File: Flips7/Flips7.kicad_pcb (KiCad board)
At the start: 2 copper layers, 100 x 100 mm, 20 parts, among them CN1 Conn_02x17_Odd_Even, CN2 Conn_02x17_Odd_Even, U1 FP2800A, U2 FP2800A, U3 FP2800A

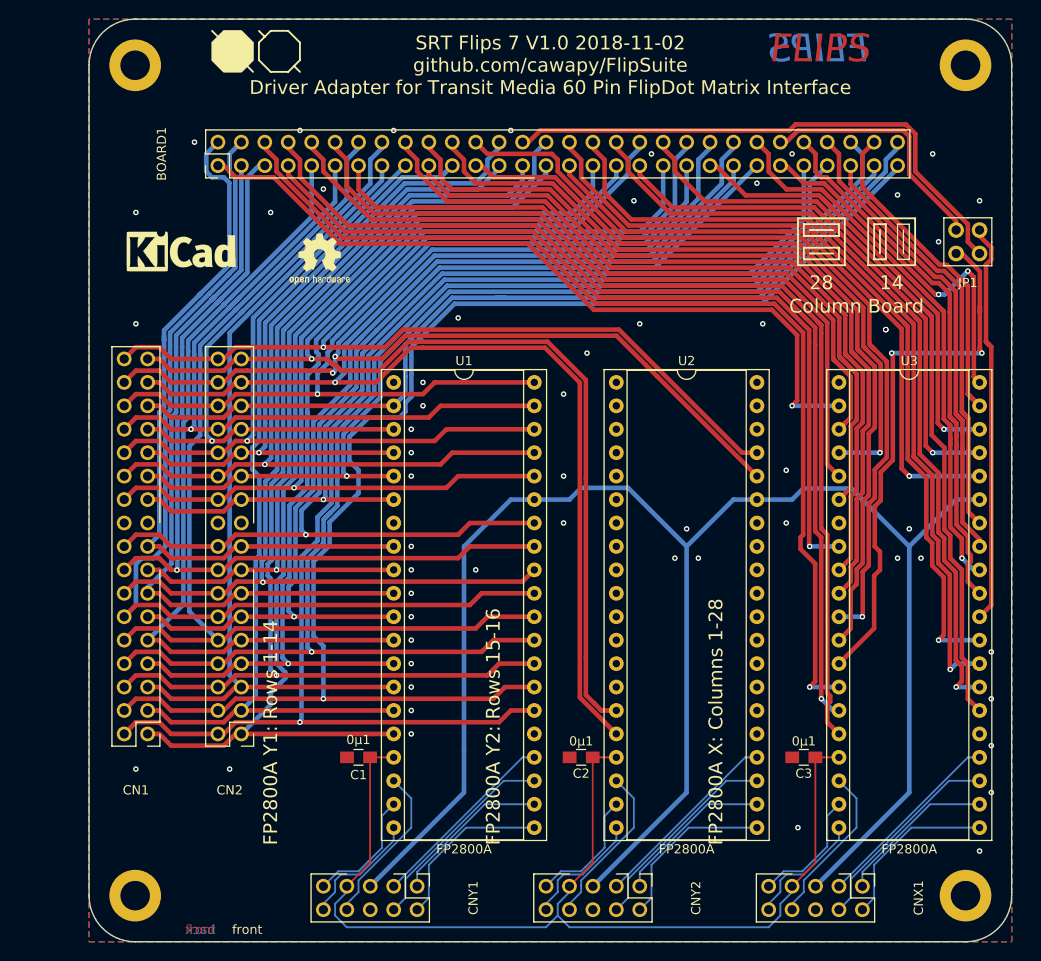
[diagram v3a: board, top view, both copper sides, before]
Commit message: moving text, adding lines to visually group driver ics and corresponding connectors
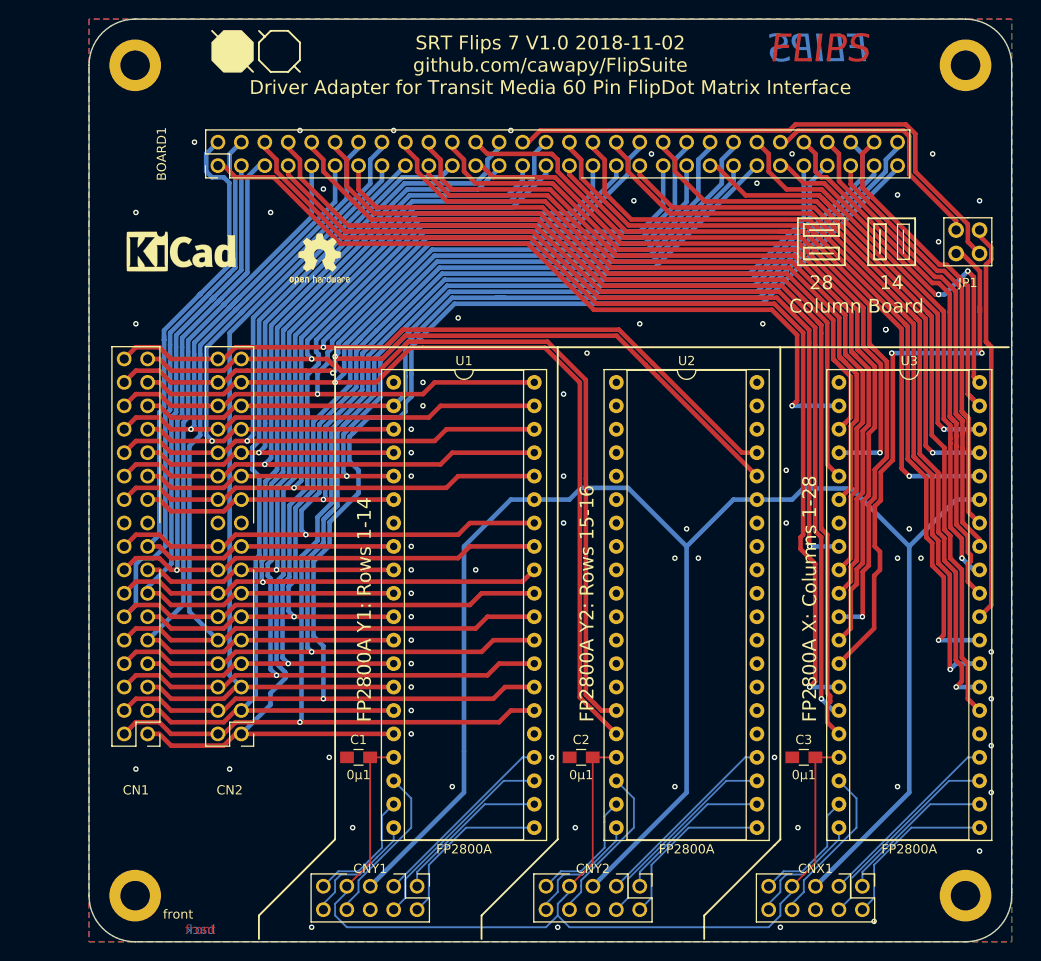
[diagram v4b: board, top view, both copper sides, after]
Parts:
- moved REF*** 48.3 mm to (30.5, 110.5)
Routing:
- net /GND: vias 56 -> 68
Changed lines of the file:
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@@
   (general
     (thickness 1.6)
-    (drawings 64)
-    (tracks 1399)
+    (drawings 76)
+    (tracks 1411)
     (zones 0)
     (modules 20)
@@
   )
   (layers
-    (0 F.Cu signal hide)
+    (0 F.Cu signal)
     (31 B.Cu signal)
     (32 B.Adhes user)
@@
     (34 B.Paste user)
     (35 F.Paste user)
-    (36 B.SilkS user hide)
-    (37 F.SilkS user hide)
+    (36 B.SilkS user)
+    (37 F.SilkS user)
     (38 B.Mask user)
     (39 F.Mask user)
@@
     (46 B.CrtYd user)
     (47 F.CrtYd user)
-    (48 B.Fab user hide)
-    (49 F.Fab user hide)
+    (48 B.Fab user)
+    (49 F.Fab user)
   )
   (setup
@@
     (tags "capacitor 0805")
     (attr smd)
-    (fp_text reference C2 (at 0 -1.75 180) (layer F.SilkS)
+    (fp_text reference C2 (at 0 1.905 180) (layer F.SilkS)
       (effects (font (size 1 1) (thickness 0.15)))
     )
-    (fp_text value 0µ1 (at 0 1.75 180) (layer F.SilkS)
+    (fp_text value 0µ1 (at 0 -1.905 180) (layer F.SilkS)
       (effects (font (size 1 1) (thickness 0.15)))
     )
@@
     (fp_line (start 1 0.62) (end -1 0.62) (layer F.Fab) (width 0.1))
     (fp_line (start -1 0.62) (end -1 -0.62) (layer F.Fab) (width 0.1))
-    (fp_text user %R (at 0 -1.75 180) (layer F.Fab)
+    (fp_text user %R (at 0 1.905 180) (layer F.Fab)
       (effects (font (size 1 1) (thickness 0.15)))
     )
@@
     (tags "capacitor 0805")
     (attr smd)
-    (fp_text reference C3 (at 0 -1.75 180) (layer F.SilkS)
+    (fp_text reference C3 (at 0 1.905 180) (layer F.SilkS)
       (effects (font (size 1 1) (thickness 0.15)))
     )
-    (fp_text value 0µ1 (at 0 1.75 180) (layer F.SilkS)
+    (fp_text value 0µ1 (at 0 -1.905 180) (layer F.SilkS)
       (effects (font (size 1 1) (thickness 0.15)))
     )
@@
     (fp_line (start 1 0.62) (end -1 0.62) (layer F.Fab) (width 0.1))
     (fp_line (start -1 0.62) (end -1 -0.62) (layer F.Fab) (width 0.1))
-    (fp_text user %R (at 0 -1.75 180) (layer F.Fab)
+    (fp_text user %R (at 0 1.905 180) (layer F.Fab)
       (effects (font (size 1 1) (thickness 0.15)))
     )
@@
   )
   (module Symbols:WEEE-Logo_4.2x6mm_SilkScreen (layer B.Cu)
-    (at 78.105 118.745 180)
+    (at 30.48 110.49 180)
     (descr "Waste Electrical and Electronic Equipment Directive")
     (tags "Logo WEEE")
@@
     (tags "capacitor 0805")
     (attr smd)
-    (fp_text reference C1 (at 0 1.905) (layer F.SilkS)
+    (fp_text reference C1 (at 0 -1.905) (layer F.SilkS)
       (effects (font (size 1 1) (thickness 0.15)))
     )
-    (fp_text value 0µ1 (at -0.02 -1.905) (layer F.SilkS)
+    (fp_text value 0µ1 (at 0 1.905) (layer F.SilkS)
       (effects (font (size 1 1) (thickness 0.15)))
     )
@@
     (fp_line (start 1 0.62) (end -1 0.62) (layer F.Fab) (width 0.1))
     (fp_line (start -1 0.62) (end -1 -0.62) (layer F.Fab) (width 0.1))
-    (fp_text user %R (at 0 -1.75) (layer F.Fab)
+    (fp_text user %R (at 0 -1.905) (layer F.Fab)
       (effects (font (size 1 1) (thickness 0.15)))
     )
@@
     (descr "Through hole shrouded angle pin header, 2x05, 2.54mm pitch, double rows, conventional numbering")
     (tags "Through hole shrouded angle pin header THT 2x05 2.54mm double row, conventional numbering")
-    (fp_text reference CNX1 (at 1.27 -6.096 270) (layer F.SilkS)
+    (fp_text reference CNX1 (at -1.905 5.08) (layer F.SilkS)
       (effects (font (size 1 1) (thickness 0.15)))
     )
@@
     (descr "Through hole shrouded angle pin header, 2x05, 2.54mm pitch, double rows, conventional numbering")
     (tags "Through hole shrouded angle pin header THT 2x05 2.54mm double row, conventional numbering")
-    (fp_text reference CNY1 (at 1.27 -6.096 270) (layer F.SilkS)
+    (fp_text reference CNY1 (at -1.905 5.08) (layer F.SilkS)
       (effects (font (size 1 1) (thickness 0.15)))
     )
@@
     (descr "Through hole shrouded angle pin header, 2x05, 2.54mm pitch, double rows, conventional numbering")
     (tags "Through hole shrouded angle pin header THT 2x05 2.54mm double row, conventional numbering")
-    (fp_text reference CNY2 (at 1.27 -6.096 270) (layer F.SilkS)
+    (fp_text reference CNY2 (at -1.905 5.08) (layer F.SilkS)
       (effects (font (size 1 1) (thickness 0.15)))
     )
@@
     (pad 1 thru_hole circle (at 0 0) (size 5.6 5.6) (drill 3.2) (layers *.Cu *.Mask))
   )
+  (gr_line (start 52.07 60.96) (end 125.095 60.96) (angle 90) (layer F.SilkS) (width 0.2))
+  (gr_line (start 52.07 114.3) (end 52.07 60.96) (angle 90) (layer F.SilkS) (width 0.2))
+  (gr_line (start 43.815 122.555) (end 52.07 114.3) (angle 90) (layer F.SilkS) (width 0.2))
+  (gr_line (start 43.815 125.095) (end 43.815 122.555) (angle 90) (layer F.SilkS) (width 0.2))
+  (gr_line (start 76.2 114.3) (end 76.2 60.96) (angle 90) (layer F.SilkS) (width 0.2))
+  (gr_line (start 67.945 122.555) (end 76.2 114.3) (angle 90) (layer F.SilkS) (width 0.2))
+  (gr_line (start 67.945 125.095) (end 67.945 122.555) (angle 90) (layer F.SilkS) (width 0.2))
+  (gr_line (start 100.33 114.3) (end 100.33 60.96) (angle 90) (layer F.SilkS) (width 0.2))
+  (gr_line (start 99.695 114.935) (end 100.33 114.3) (angle 90) (layer F.SilkS) (width 0.2))
+  (gr_line (start 92.075 123.825) (end 92.075 125.095) (angle 90) (layer F.SilkS) (width 0.2))
+  (gr_line (start 92.075 122.555) (end 92.075 123.825) (angle 90) (layer F.SilkS) (width 0.2))
+  (gr_line (start 99.695 114.935) (end 92.075 122.555) (angle 90) (layer F.SilkS) (width 0.2))
   (gr_text "Column Board" (at 108.585 56.515) (layer F.SilkS)
     (effects (font (size 1.5 1.5) (thickness 0.3)))
   )
-  (gr_text "FP2800A X: Columns 1-28" (at 93.345 114.935 90) (layer F.SilkS)
+  (gr_text "FP2800A X: Columns 1-28" (at 103.505 101.6 90) (layer F.SilkS)
     (effects (font (size 1.5 1.5) (thickness 0.3)) (justify left))
   )
@@
   (gr_arc (start 120.4 30.4) (end 125.4 30.4) (angle -90) (layer Edge.Cuts) (width 0.15))
   (gr_arc (start 30.4 30.4) (end 30.4 25.4) (angle -90) (layer Edge.Cuts) (width 0.15))
-  (gr_text back (at 42.545 124.079) (layer B.SilkS)
+  (gr_text back (at 35.052 122.428) (layer B.SilkS)
     (effects (font (size 1 1) (thickness 0.25)) (justify mirror))
   )
@@
     (effects (font (size 1 1) (thickness 0.25)) (justify mirror))
   )
-  (gr_text front (at 42.545 124.079) (layer F.SilkS)
+  (gr_text front (at 35.052 122.428) (layer F.SilkS)
     (effects (font (size 1 1) (thickness 0.25)))
   )
@@
     (effects (font (size 1.5 1.5) (thickness 0.3)))
   )
-  (gr_text "FP2800A Y1: Rows 1-14" (at 45.085 114.935 90) (layer F.SilkS)
+  (gr_text "FP2800A Y1: Rows 1-14" (at 55.245 101.6 90) (layer F.SilkS)
     (effects (font (size 1.5 1.5) (thickness 0.3)) (justify left))
   )
-  (gr_text "FP2800A Y2: Rows 15-16" (at 69.215 114.935 90) (layer F.SilkS)
+  (gr_text "FP2800A Y2: Rows 15-16" (at 79.375 101.6 90) (layer F.SilkS)
     (effects (font (size 1.5 1.5) (thickness 0.3)) (justify left))
   )
@@
   (via (at 76.835 74.93) (size 0.6) (drill 0.3) (layers F.Cu B.Cu) (net 112))
   (via (at 100.965 80.01) (size 0.6) (drill 0.3) (layers F.Cu B.Cu) (net 112))
+  (via (at 51.435 105.41) (size 0.6) (drill 0.3) (layers F.Cu B.Cu) (net 112))
+  (via (at 75.565 105.41) (size 0.6) (drill 0.3) (layers F.Cu B.Cu) (net 112))
+  (via (at 99.695 105.41) (size 0.6) (drill 0.3) (layers F.Cu B.Cu) (net 112))
+  (via (at 78.105 113.03) (size 0.6) (drill 0.3) (layers F.Cu B.Cu) (net 112))
+  (via (at 53.975 113.03) (size 0.6) (drill 0.3) (layers F.Cu B.Cu) (net 112))
+  (via (at 64.77 108.585) (size 0.6) (drill 0.3) (layers F.Cu B.Cu) (net 112))
+  (via (at 88.9 108.585) (size 0.6) (drill 0.3) (layers F.Cu B.Cu) (net 112))
+  (via (at 113.03 108.585) (size 0.6) (drill 0.3) (layers F.Cu B.Cu) (net 112))
+  (via (at 110.49 123.19) (size 0.6) (drill 0.3) (layers F.Cu B.Cu) (net 112))
+  (via (at 100.33 123.825) (size 0.6) (drill 0.3) (layers F.Cu B.Cu) (net 112))
+  (via (at 76.2 123.825) (size 0.6) (drill 0.3) (layers F.Cu B.Cu) (net 112))
+  (via (at 49.53 123.825) (size 0.6) (drill 0.3) (layers F.Cu B.Cu) (net 112))
   (segment (start 66.04 104.775) (end 66.04 82.55) (width 0.5) (layer B.Cu) (net 113) (status 10))
   (segment (start 71.12 77.47) (end 73.66 77.47) (width 0.5) (layer B.Cu) (net 113) (status 20))

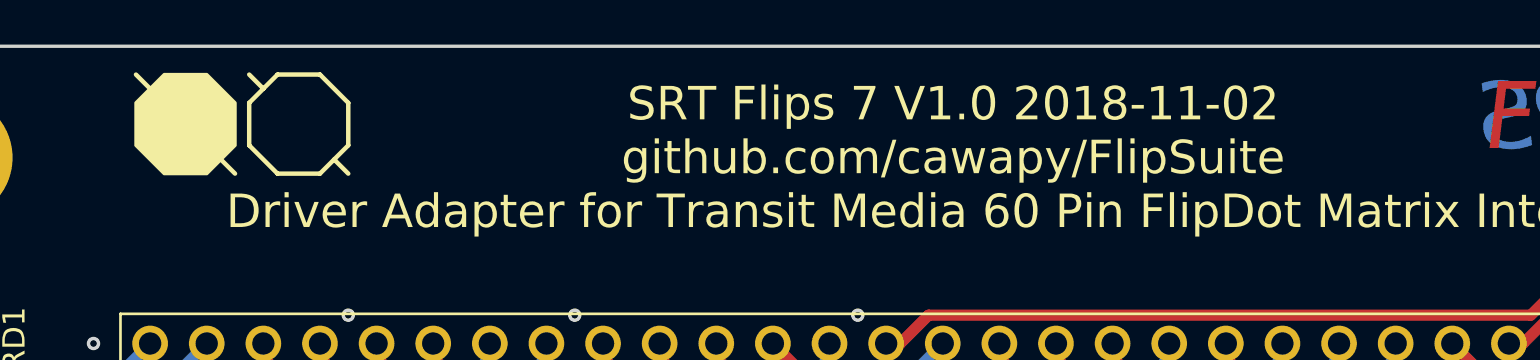
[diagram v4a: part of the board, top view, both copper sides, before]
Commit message: Adding Flips Logo
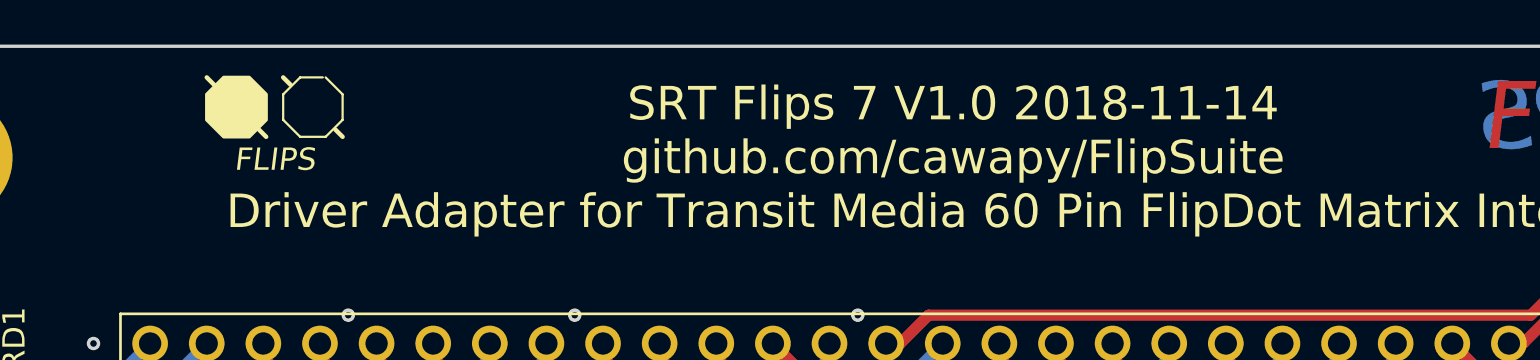
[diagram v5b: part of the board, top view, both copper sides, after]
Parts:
- added REF**: FlipsLogo-Mittel, Own:FlipsLogo-Mittel, F.Cu at (45.0, 29.5)
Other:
- board text added: "SRT Flips 7 V1.0 2018-11-14 github.com/cawapy/FlipSuite Driver Adapter for Transit Media 60 Pin FlipDot Matrix Interface"
- board text removed: "SRT Flips 7 V1.0 2018-11-02 github.com/cawapy/FlipSuite Driver Adapter for Transit Media 60 Pin FlipDot Matrix Interface"
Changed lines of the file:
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@@
   (general
     (thickness 1.6)
-    (drawings 76)
+    (drawings 63)
     (tracks 1411)
     (zones 0)
-    (modules 20)
+    (modules 21)
     (nets 114)
   )
@@
     (zone_45_only no)
     (trace_min 0.2)
-    (segment_width 0.2)
+    (segment_width 0.4)
     (edge_width 0.15)
     (via_size 0.6)
@@
     (aux_axis_origin 0 0)
     (grid_origin 25.4 25.4)
-    (visible_elements 7FFFFFFF)
+    (visible_elements 7FF7FFFF)
     (pcbplotparams
       (layerselection 0x010f0_ffffffff)
@@
     (pad 1 thru_hole circle (at 0 0) (size 5.6 5.6) (drill 3.2) (layers *.Cu *.Mask))
   )
+  (module Own:FlipsLogo-Mittel (layer F.Cu)
+    (at 44.958 29.464)
+    (fp_text reference REF** (at 0 3.81) (layer F.Fab) hide
+      (effects (font (size 1 1) (thickness 0.15)))
+    )
+    (fp_text value FlipsLogo-Mittel (at 0 2.54) (layer F.Fab)
+      (effects (font (size 1 1) (thickness 0.15)))
+    )
+    (fp_line (start -0.381 0) (end -0.6985 -0.3175) (layer F.SilkS) (width 0.2))
+    (fp_line (start -3.048 -2.667) (end -2.7178 -2.3368) (layer F.SilkS) (width 0.2))
+    (fp_line (start -3.048 1.778) (end -3.048 -2.667) (layer F.CrtYd) (width 0.1))
+    (fp_line (start 3.048 1.778) (end -3.048 1.778) (layer F.CrtYd) (width 0.1))
+    (fp_line (start 3.048 -2.667) (end 3.048 1.778) (layer F.CrtYd) (width 0.1))
+    (fp_line (start -3.048 -2.667) (end 3.048 -2.667) (layer F.CrtYd) (width 0.1))
+    (fp_poly (pts (xy -0.381 -1.905) (xy -0.381 -0.762) (xy -1.143 0) (xy -2.286 0)
+      (xy -3.048 -0.762) (xy -3.048 -1.905) (xy -2.286 -2.667) (xy -1.143 -2.667)) (layer F.SilkS) (width 0.15))
+    (fp_line (start 0.381 -2.667) (end 0.7112 -2.3368) (layer F.SilkS) (width 0.2))
+    (fp_line (start 1.143 0) (end 2.286 0) (layer F.SilkS) (width 0.1))
+    (fp_line (start 0.381 -0.762) (end 1.143 0) (layer F.SilkS) (width 0.1))
+    (fp_line (start 0.381 -1.905) (end 0.381 -0.762) (layer F.SilkS) (width 0.1))
+    (fp_line (start 1.143 -2.667) (end 0.381 -1.905) (layer F.SilkS) (width 0.1))
+    (fp_line (start 2.159 -2.667) (end 1.143 -2.667) (layer F.SilkS) (width 0.1))
+    (fp_line (start 3.048 -1.905) (end 2.286 -2.667) (layer F.SilkS) (width 0.1))
+    (fp_line (start 3.048 -0.762) (end 3.048 -1.905) (layer F.SilkS) (width 0.1))
+    (fp_line (start 2.286 0) (end 3.048 -0.762) (layer F.SilkS) (width 0.1))
+    (fp_line (start 3.048 0) (end 2.7305 -0.3175) (layer F.SilkS) (width 0.2))
+    (fp_text user FLIPS (at 0 1.016) (layer F.SilkS)
+      (effects (font (size 1 1) (thickness 0.2) italic))
+    )
+  )
   (gr_line (start 52.07 60.96) (end 125.095 60.96) (angle 90) (layer F.SilkS) (width 0.2))
   (gr_line (start 52.07 114.3) (end 52.07 60.96) (angle 90) (layer F.SilkS) (width 0.2))
@@
     (effects (font (size 1.5 1.5) (thickness 0.3)) (justify left))
   )
-  (gr_line (start 47.625 30.48) (end 48.26 31.115) (layer F.SilkS) (width 0.2))
-  (gr_line (start 45.085 26.67) (end 44.45 27.305) (layer F.SilkS) (width 0.2))
-  (gr_line (start 46.99 26.67) (end 45.085 26.67) (layer F.SilkS) (width 0.2))
-  (gr_line (start 48.26 27.94) (end 46.99 26.67) (layer F.SilkS) (width 0.2))
-  (gr_line (start 48.26 29.845) (end 48.26 27.94) (layer F.SilkS) (width 0.2))
-  (gr_line (start 46.99 31.115) (end 48.26 29.845) (layer F.SilkS) (width 0.2))
-  (gr_line (start 45.085 31.115) (end 46.99 31.115) (layer F.SilkS) (width 0.2))
-  (gr_line (start 43.815 29.845) (end 45.085 31.115) (layer F.SilkS) (width 0.2))
-  (gr_line (start 43.815 27.94) (end 43.815 29.845) (layer F.SilkS) (width 0.2))
-  (gr_line (start 44.45 27.305) (end 43.815 27.94) (layer F.SilkS) (width 0.2))
-  (gr_line (start 43.815 26.67) (end 44.45 27.305) (layer F.SilkS) (width 0.2))
-  (gr_line (start 38.735 26.67) (end 43.18 31.115) (layer F.SilkS) (width 0.2))
-  (gr_poly (pts (xy 38.735 27.94) (xy 40.005 26.67) (xy 41.91 26.67) (xy 43.18 27.94) (xy 43.18 29.845) (xy 41.91 31.115) (xy 40.005 31.115) (xy 38.735 29.845)) (layer F.SilkS) (width 0.15))
   (gr_text 14 (at 112.395 53.975) (layer F.SilkS)
     (effects (font (size 1.5 1.5) (thickness 0.3)))
@@
     (effects (font (size 3 3) (thickness 0.75) italic) (justify left))
   )
-  (gr_text "SRT Flips 7 V1.0 2018-11-02\ngithub.com/cawapy/FlipSuite\nDriver Adapter for Transit Media 60 Pin FlipDot Matrix Interface" (at 75.4 30.4) (layer F.SilkS)
+  (gr_text "SRT Flips 7 V1.0 2018-11-14\ngithub.com/cawapy/FlipSuite\nDriver Adapter for Transit Media 60 Pin FlipDot Matrix Interface" (at 75.4 30.4) (layer F.SilkS)
     (effects (font (size 1.5 1.5) (thickness 0.3)))
   )

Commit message: finer routing
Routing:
- net /~SY04: track 113.6 -> 136.4 mm
- net /X22: track 83.5 -> 87.8 mm
- net /RY15: track 133.1 -> 137.2 mm
- net /RY04: track 101.6 -> 104.8 mm
- net /~SY15: track 148.8 -> 152.0 mm
- net /X18: track 40.6 -> 38.0 mm
- net /RY11: track 149.2 -> 146.8 mm
- net /X28: track 59.2 -> 61.3 mm
- net /RY09: track 154.1 -> 152.7 mm
- net /X04: track 60.1 -> 58.8 mm
- net /X19: track 46.0 -> 44.7 mm
- net /~SY11: track 99.4 -> 100.6 mm, vias 0 -> 1
- net /X21: track 52.0 -> 50.8 mm
- net /~SY16: track 139.6 -> 138.5 mm
- net /X26: track 58.4 -> 57.3 mm
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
